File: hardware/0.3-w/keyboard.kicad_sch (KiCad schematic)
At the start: 267 parts, among them J1 USB_C_Receptacle_USB2.0, J2 SWD, J3 JST_PH2, Q1 AO3401A, Q2 2N7002, Q3 2N7002, SW1 RESET, U1 TP4057, U2 SRV05-4, U3 XC6206PxxxMR, U4 nRF52840_holyiot_18010

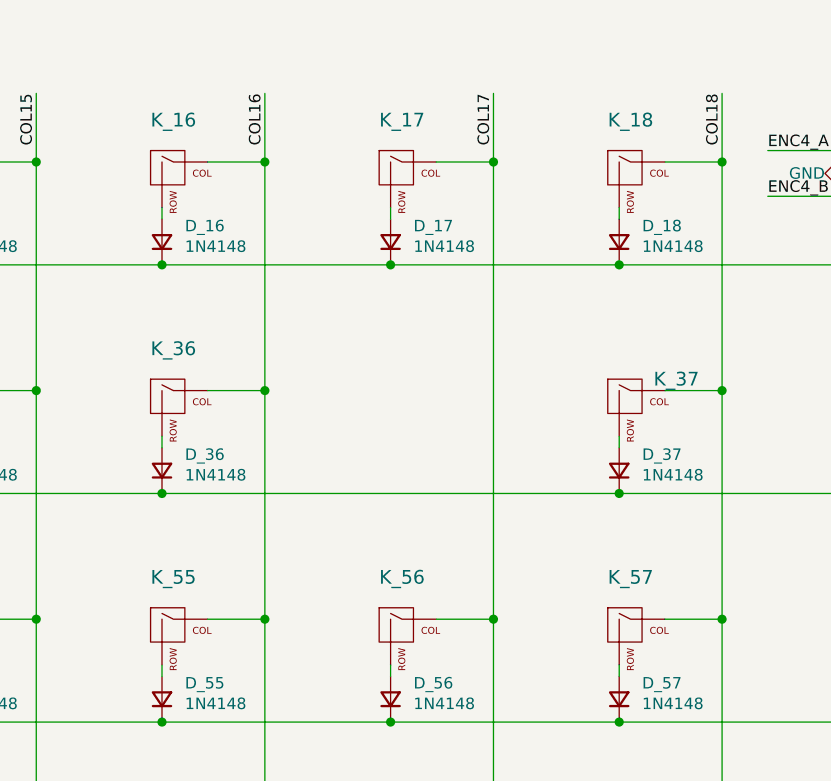
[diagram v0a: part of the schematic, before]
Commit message: all parts placed
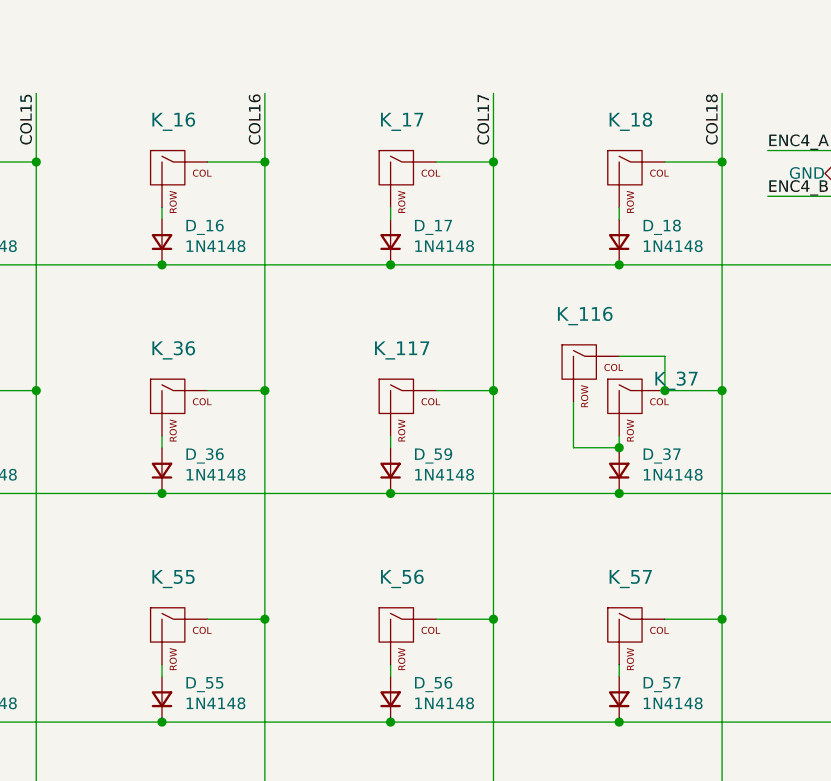
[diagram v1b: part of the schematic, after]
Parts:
- added D_59: 1N4148, Diode_SMD:D_SOD-123, symbol Device:D_Small
- added K_116, K_117: KEYSW, josh-keyboard:MXOnly-1U-NoLED, symbol josh-keyboard:MX-NoLED
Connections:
- net COL17: now also K_117.1 (COL)
- net COL18: now also K_116.1 (COL)
- net ROW1: now also D_59.1 (K)
- net at D_37.2 (A), K_37.2 (ROW): now also K_116.2 (ROW)
- new net: D_59.2 (A), K_117.2 (ROW)
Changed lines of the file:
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@@
   (junction (at 487.68 170.18) (diameter 1.016) (color 0 0 0 0))
   (junction (at 501.65 58.42) (diameter 1.016) (color 0 0 0 0))
+  (junction (at 501.65 83.82) (diameter 1.016) (color 0 0 0 0))
   (junction (at 501.65 109.22) (diameter 1.016) (color 0 0 0 0))
   (junction (at 501.65 134.62) (diameter 1.016) (color 0 0 0 0))
@@
   (junction (at 501.65 185.42) (diameter 1.016) (color 0 0 0 0))
   (junction (at 513.08 46.99) (diameter 1.016) (color 0 0 0 0))
+  (junction (at 513.08 72.39) (diameter 1.016) (color 0 0 0 0))
   (junction (at 513.08 97.79) (diameter 1.016) (color 0 0 0 0))
   (junction (at 513.08 123.19) (diameter 1.016) (color 0 0 0 0))
   (junction (at 513.08 148.59) (diameter 1.016) (color 0 0 0 0))
   (junction (at 527.05 58.42) (diameter 1.016) (color 0 0 0 0))
+  (junction (at 527.05 78.74) (diameter 1.016) (color 0 0 0 0))
   (junction (at 527.05 83.82) (diameter 1.016) (color 0 0 0 0))
   (junction (at 527.05 109.22) (diameter 1.016) (color 0 0 0 0))
   (junction (at 527.05 160.02) (diameter 1.016) (color 0 0 0 0))
   (junction (at 527.05 185.42) (diameter 1.016) (color 0 0 0 0))
+  (junction (at 532.13 72.39) (diameter 1.016) (color 0 0 0 0))
   (junction (at 538.48 46.99) (diameter 1.016) (color 0 0 0 0))
   (junction (at 538.48 72.39) (diameter 1.016) (color 0 0 0 0))
@@
     (stroke (width 0) (type solid) (color 0 0 0 0))
   )
-  (wire (pts (xy 476.25 83.82) (xy 527.05 83.82))
+  (wire (pts (xy 476.25 83.82) (xy 501.65 83.82))
     (stroke (width 0) (type solid) (color 0 0 0 0))
   )
@@
     (stroke (width 0) (type solid) (color 0 0 0 0))
   )
+  (wire (pts (xy 501.65 77.47) (xy 501.65 78.74))
+    (stroke (width 0) (type solid) (color 0 0 0 0))
+  )
+  (wire (pts (xy 501.65 83.82) (xy 527.05 83.82))
+    (stroke (width 0) (type solid) (color 0 0 0 0))
+  )
   (wire (pts (xy 501.65 102.87) (xy 501.65 104.14))
     (stroke (width 0) (type solid) (color 0 0 0 0))
@@
     (stroke (width 0) (type solid) (color 0 0 0 0))
   )
+  (wire (pts (xy 506.73 72.39) (xy 513.08 72.39))
+    (stroke (width 0) (type solid) (color 0 0 0 0))
+  )
   (wire (pts (xy 506.73 97.79) (xy 513.08 97.79))
     (stroke (width 0) (type solid) (color 0 0 0 0))
@@
     (stroke (width 0) (type solid) (color 0 0 0 0))
   )
-  (wire (pts (xy 513.08 46.99) (xy 513.08 97.79))
+  (wire (pts (xy 513.08 46.99) (xy 513.08 72.39))
+    (stroke (width 0) (type solid) (color 0 0 0 0))
+  )
+  (wire (pts (xy 513.08 72.39) (xy 513.08 97.79))
     (stroke (width 0) (type solid) (color 0 0 0 0))
   )
@@
     (stroke (width 0) (type solid) (color 0 0 0 0))
   )
+  (wire (pts (xy 521.97 73.66) (xy 521.97 78.74))
+    (stroke (width 0) (type solid) (color 0 0 0 0))
+  )
+  (wire (pts (xy 521.97 78.74) (xy 527.05 78.74))
+    (stroke (width 0) (type solid) (color 0 0 0 0))
+  )
   (wire (pts (xy 527.05 52.07) (xy 527.05 53.34))
     (stroke (width 0) (type solid) (color 0 0 0 0))
@@
     (stroke (width 0) (type solid) (color 0 0 0 0))
   )
+  (wire (pts (xy 527.05 68.58) (xy 532.13 68.58))
+    (stroke (width 0) (type solid) (color 0 0 0 0))
+  )
   (wire (pts (xy 527.05 77.47) (xy 527.05 78.74))
     (stroke (width 0) (type solid) (color 0 0 0 0))
@@
     (stroke (width 0) (type solid) (color 0 0 0 0))
   )
+  (wire (pts (xy 532.13 68.58) (xy 532.13 72.39))
+    (stroke (width 0) (type solid) (color 0 0 0 0))
+  )
   (wire (pts (xy 532.13 72.39) (xy 538.48 72.39))
     (stroke (width 0) (type solid) (color 0 0 0 0))
@@
     (pin "2")
   )
+  (symbol (lib_id "Device:D_Small") (at 501.65 81.28 90) (unit 1)
+    (in_bom yes) (on_board yes)
+    (property "Reference" "D_59" (id 0) (at 504.19 79.502 90)
+      (effects (font (size 1.27 1.27)) (justify right))
+    )
+    (property "Value" "1N4148" (id 1) (at 504.19 81.788 90)
+      (effects (font (size 1.27 1.27)) (justify right))
+    )
+    (property "Footprint" "Diode_SMD:D_SOD-123" (id 2) (at 502.92 88.9 0)
+      (effects (font (size 1.27 1.27)) hide)
+    )
+    (property "Datasheet" "~" (id 3) (at 502.92 88.9 0)
+      (effects (font (size 1.27 1.27)) hide)
+    )
+    (property "JLCSMT" "C81598" (id 4) (at 501.65 81.28 0)
+      (effects (font (size 1.27 1.27)) hide)
+    )
+    (property "LCSC" "C81598" (id 5) (at 501.65 81.28 0)
+      (effects (font (size 1.27 1.27)) hide)
+    )
+    (property "MPN" "1N4148W" (id 6) (at 501.65 81.28 0)
+      (effects (font (size 1.27 1.27)) hide)
+    )
+    (property "Manufacturer" "Semtech" (id 7) (at 501.65 81.28 0)
+      (effects (font (size 1.27 1.27)) hide)
+    )
+    (pin "1")
+    (pin "2")
+  )
   (symbol (lib_id "Device:D_Small") (at 501.65 106.68 90) (unit 1)
     (in_bom yes) (on_board yes)
@@
     (pin "2")
   )
+  (symbol (lib_id "josh-keyboard:MX-NoLED") (at 502.92 73.66 0) (unit 1)
+    (in_bom yes) (on_board yes)
+    (property "Reference" "K_117" (id 0) (at 502.92 67.7418 0)
+      (effects (font (size 1.524 1.524)))
+    )
+    (property "Value" "KEYSW" (id 1) (at 502.92 76.2 0)
+      (effects (font (size 1.524 1.524)) hide)
+    )
+    (property "Footprint" "josh-keyboard:MXOnly-1U-NoLED" (id 2) (at 502.92 73.66 0)
+      (effects (font (size 1.524 1.524)) hide)
+    )
+    (property "Datasheet" "" (id 3) (at 502.92 73.66 0)
+      (effects (font (size 1.524 1.524)))
+    )
+    (property "DNP" "DNP" (id 4) (at 502.92 73.66 0)
+      (effects (font (size 1.27 1.27)) hide)
+    )
+    (pin "1")
+    (pin "2")
+  )
   (symbol (lib_id "josh-keyboard:MX-NoLED") (at 502.92 99.06 0) (unit 1)
     (in_bom yes) (on_board yes)
@@
     (pin "2")
   )
+  (symbol (lib_id "josh-keyboard:MX-NoLED") (at 523.24 69.85 0) (unit 1)
+    (in_bom yes) (on_board yes)
+    (property "Reference" "K_116" (id 0) (at 523.24 63.9318 0)
+      (effects (font (size 1.524 1.524)))
+    )
+    (property "Value" "KEYSW" (id 1) (at 523.24 72.39 0)
+      (effects (font (size 1.524 1.524)) hide)
+    )
+    (property "Footprint" "josh-keyboard:MXOnly-1U-NoLED" (id 2) (at 523.24 69.85 0)
+      (effects (font (size 1.524 1.524)) hide)
+    )
+    (property "Datasheet" "" (id 3) (at 523.24 69.85 0)
+      (effects (font (size 1.524 1.524)))
+    )
+    (property "DNP" "DNP" (id 4) (at 523.24 69.85 0)
+      (effects (font (size 1.27 1.27)) hide)
+    )
+    (pin "1")
+    (pin "2")
+  )
   (symbol (lib_id "josh-keyboard:MX-NoLED") (at 528.32 48.26 0) (unit 1)
     (in_bom yes) (on_board yes)
@@
       (reference "D_58") (unit 1) (value "1N4148") (footprint "Diode_SMD:D_SOD-123")
     )
+    (path "/cb42b9bb-fc46-4c19-b315-048646672a96"
+      (reference "D_59") (unit 1) (value "1N4148") (footprint "Diode_SMD:D_SOD-123")
+    )
     (path "/00000000-0000-0000-0000-000000000600"
       (reference "D_60") (unit 1) (value "1N4148") (footprint "Diode_SMD:D_SOD-123")
@@
       (reference "K_115") (unit 1) (value "KEYSW") (footprint "josh-keyboard:MXOnly-1U-NoLED")
     )
+    (path "/a53bcfa5-987c-4dbc-9743-d5bb1d285c81"
+      (reference "K_116") (unit 1) (value "KEYSW") (footprint "josh-keyboard:MXOnly-1U-NoLED")
+    )
+    (path "/3eab3946-b5c2-4325-8805-84ddc6f65b8a"
+      (reference "K_117") (unit 1) (value "KEYSW") (footprint "josh-keyboard:MXOnly-1U-NoLED")
+    )
     (path "/00000000-0000-0000-0000-0000619339fa"

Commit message: drc = erc = 0
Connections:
- net COL0: now also U4.36 (P0.10)
- net COL1: now also U4.6 (P0.03)
- net COL10: now also U4.27 (P1.00)
- net COL11: now also U4.26 (P0.22)
- net COL12: now also U4.39 (P1.12)
- net COL13: now also U4.47 (P1.07)
- net COL14: now also U4.48 (P1.05)
- net COL15: now also U4.34 (P1.06)
- net COL16: now also U4.49 (P0.24)
- net COL17: now also U4.33 (P1.04)
- net COL18: now also U4.50 (P0.20)
- net COL19: now also U4.51 (P0.17)
- net COL2: now also U4.15 (P0.07)
- net COL3: now also U4.16 (P1.09)
- net COL4: now also U4.35 (P0.09)
- net COL5: now also U4.38 (P1.14)
- net COL6: now also U4.30 (P1.02)
- net COL7: now also U4.29 (P1.01)
- net COL8: now also U4.53 (P0.14)
- net COL9: now also U4.28 (P1.03)
- net ENC0_A: now also U4.7 (P0.02)
- net ENC0_B: now also U4.8 (P0.28)
- net ENC1_A: now also U4.9 (P0.29)
- net ENC1_B: now also U4.10 (P0.30)
- net ENC2_A: now also U4.17 (P0.12)
- net ENC2_B: now also U4.18 (P0.23)
- net ENC3_A: now also U4.19 (P0.21)
- net ENC3_B: now also U4.20 (P0.19)
- net ENC4_A: now also U4.55 (P0.16)
- net ENC4_B: now also U4.54 (P0.13)
- net ROW0: now also U4.46 (P0.26)
- net ROW1: now also U4.45 (P0.06)
- net ROW2: now also U4.43 (P0.27)
- net ROW3: now also U4.42 (P1.08)
- net ROW4: now also U4.41 (P0.11)
- net ROW5: now also U4.40 (P0.25)
- no-connect marks 4 -> 11

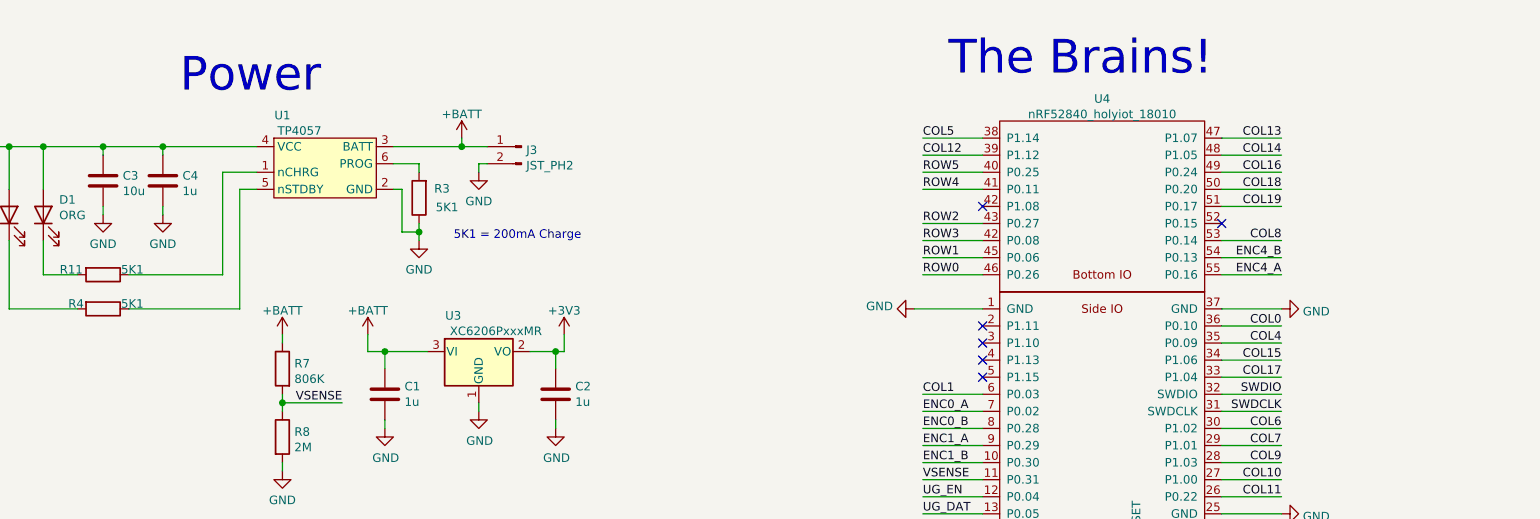
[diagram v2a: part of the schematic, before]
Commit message: added user led
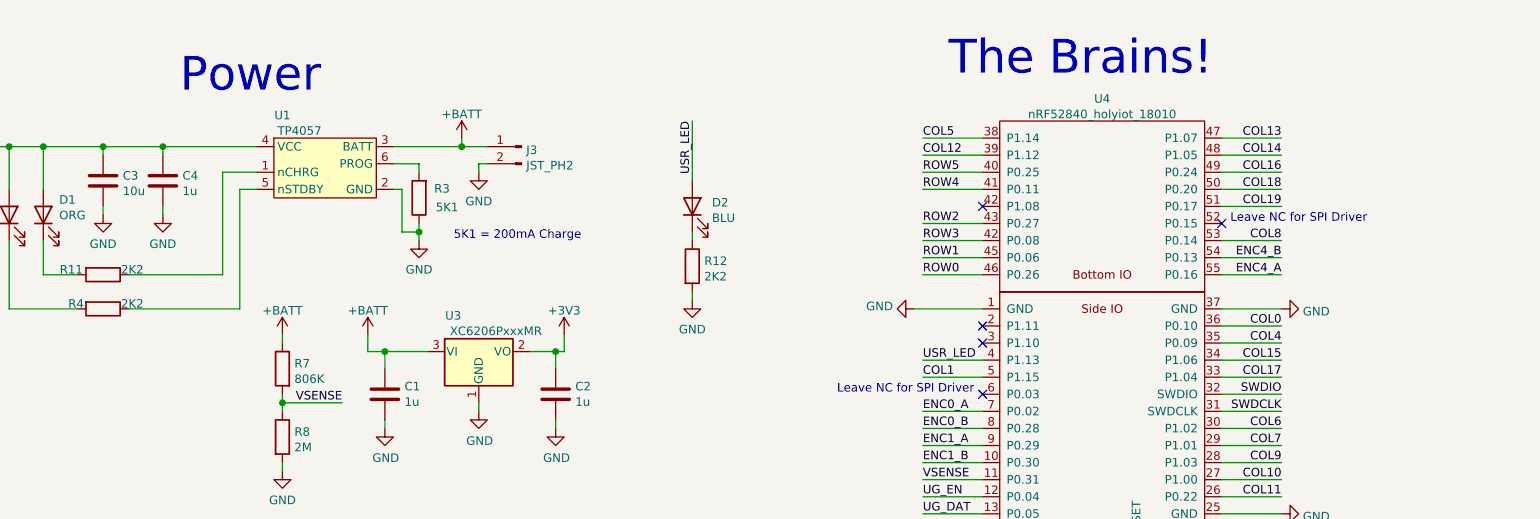
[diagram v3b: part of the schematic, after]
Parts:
- added D2: BLU, LED_SMD:LED_0603_1608Metric, symbol Device:LED
- added R12: 2K2, Resistor_SMD:R_0603_1608Metric, symbol Device:R
- R11, R4: value 5K1 -> 2K2
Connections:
- net COL1: now also U4.5 (P1.15); no longer U4.6 (P0.03)
- net GND: now also R12.2
- net USR_LED: now reaches U4.4 (P1.13)
- net USR_LED: now also D2.2 (A)
- new net: D2.1 (K), R12.1
- no-connect marks 11 -> 10
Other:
- note added: "Leave NC for SPI Driver"
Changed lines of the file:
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@@
   (no_connect (at 350.52 265.43))
   (no_connect (at 350.52 267.97))
-  (no_connect (at 350.52 270.51))
-  (no_connect (at 350.52 273.05))
+  (no_connect (at 350.52 275.59))
   (no_connect (at 386.08 250.19))
   (wire (pts (xy 35.56 46.99) (xy 27.94 46.99))
@@
     (stroke (width 0) (type solid) (color 0 0 0 0))
   )
+  (wire (pts (xy 307.34 234.95) (xy 307.34 243.84))
+    (stroke (width 0) (type solid) (color 0 0 0 0))
+  )
+  (wire (pts (xy 307.34 251.46) (xy 307.34 252.73))
+    (stroke (width 0) (type solid) (color 0 0 0 0))
+  )
+  (wire (pts (xy 307.34 260.35) (xy 307.34 261.62))
+    (stroke (width 0) (type solid) (color 0 0 0 0))
+  )
   (wire (pts (xy 309.88 39.37) (xy 309.88 46.99))
     (stroke (width 0) (type solid) (color 0 0 0 0))
@@
     (stroke (width 0) (type solid) (color 0 0 0 0))
   )
+  (wire (pts (xy 341.63 270.51) (xy 350.52 270.51))
+    (stroke (width 0) (type solid) (color 0 0 0 0))
+  )
   (wire (pts (xy 341.63 278.13) (xy 350.52 278.13))
     (stroke (width 0) (type solid) (color 0 0 0 0))
@@
     (stroke (width 0) (type solid) (color 0 0 0 0))
   )
-  (wire (pts (xy 350.52 275.59) (xy 341.63 275.59))
+  (wire (pts (xy 350.52 273.05) (xy 341.63 273.05))
     (stroke (width 0) (type solid) (color 0 0 0 0))
   )
@@
     (effects (font (size 5.0038 5.0038)) (justify left bottom))
   )
+  (text "Leave NC for SPI Driver" (at 349.25 275.59 180)
+    (effects (font (size 1.27 1.27)) (justify right bottom))
+  )
   (text "Logos / Silk" (at 372.11 375.92 0)
     (effects (font (size 2.54 2.54)) (justify left bottom))
   )
+  (text "Leave NC for SPI Driver" (at 387.35 250.19 0)
+    (effects (font (size 1.27 1.27)) (justify left bottom))
+  )
   (text "Stopping \nERC Errors" (at 402.59 378.46 0)
     (effects (font (size 2.54 2.54)) (justify left bottom))
@@
     (effects (font (size 1.27 1.27)) (justify right bottom))
   )
+  (label "USR_LED" (at 307.34 234.95 270)
+    (effects (font (size 1.27 1.27)) (justify right bottom))
+  )
   (label "COL9" (at 309.88 39.37 270)
     (effects (font (size 1.27 1.27)) (justify right bottom))
@@
     (effects (font (size 1.27 1.27)) (justify left bottom))
   )
-  (label "COL1" (at 341.63 275.59 0)
+  (label "USR_LED" (at 341.63 270.51 0)
+    (effects (font (size 1.27 1.27)) (justify left bottom))
+  )
+  (label "COL1" (at 341.63 273.05 0)
     (effects (font (size 1.27 1.27)) (justify left bottom))
   )
@@
     (pin "1")
   )
+  (symbol (lib_id "power:GND") (at 307.34 261.62 0) (unit 1)
+    (in_bom yes) (on_board yes) (fields_autoplaced)
+    (property "Reference" "#PWR0134" (id 0) (at 307.34 267.97 0)
+      (effects (font (size 1.27 1.27)) hide)
+    )
+    (property "Value" "GND" (id 1) (at 307.34 265.9444 0))
+    (property "Footprint" "" (id 2) (at 307.34 261.62 0)
+      (effects (font (size 1.27 1.27)) hide)
+    )
+    (property "Datasheet" "" (id 3) (at 307.34 261.62 0)
+      (effects (font (size 1.27 1.27)) hide)
+    )
+    (pin "1")
+  )
   (symbol (lib_id "power:GND") (at 340.36 262.89 270) (unit 1)
     (in_bom yes) (on_board yes) (fields_autoplaced)
@@
       (effects (font (size 1.27 1.27)) (justify left))
     )
-    (property "Value" "5K1" (id 1) (at 222.377 257.048 90)
+    (property "Value" "2K2" (id 1) (at 222.377 257.048 90)
       (effects (font (size 1.27 1.27)) (justify left))
     )
@@
       (effects (font (size 1.27 1.27)) (justify left))
     )
-    (property "Value" "5K1" (id 1) (at 222.377 262.128 90)
+    (property "Value" "2K2" (id 1) (at 222.377 262.128 90)
       (effects (font (size 1.27 1.27)) (justify left))
     )
@@
     (pin "2")
   )
+  (symbol (lib_id "Device:R") (at 307.34 256.54 0) (unit 1)
+    (in_bom yes) (on_board yes) (fields_autoplaced)
+    (property "Reference" "R12" (id 0) (at 309.1181 255.7791 0)
+      (effects (font (size 1.27 1.27)) (justify left))
+    )
+    (property "Value" "2K2" (id 1) (at 309.1181 258.0778 0)
+      (effects (font (size 1.27 1.27)) (justify left))
+    )
+    (property "Footprint" "Resistor_SMD:R_0603_1608Metric" (id 2) (at 305.562 256.54 90)
+      (effects (font (size 1.27 1.27)) hide)
+    )
+    (property "Datasheet" "~" (id 3) (at 307.34 256.54 0)
+      (effects (font (size 1.27 1.27)) hide)
+    )
+    (pin "1")
+    (pin "2")
+  )
   (symbol (lib_id "Device:Polyfuse") (at 176.53 238.76 270) (unit 1)
     (in_bom yes) (on_board yes)
@@
     (pin "2")
   )
+  (symbol (lib_id "Device:LED") (at 307.34 247.65 90) (unit 1)
+    (in_bom yes) (on_board yes) (fields_autoplaced)
+    (property "Reference" "D2" (id 0) (at 310.2611 247.0796 90)
+      (effects (font (size 1.27 1.27)) (justify right))
+    )
+    (property "Value" "BLU" (id 1) (at 310.2611 249.3783 90)
+      (effects (font (size 1.27 1.27)) (justify right))
+    )
+    (property "Footprint" "LED_SMD:LED_0603_1608Metric" (id 2) (at 307.34 247.65 0)
+      (effects (font (size 1.27 1.27)) hide)
+    )
+    (property "Datasheet" "~" (id 3) (at 307.34 247.65 0)
+      (effects (font (size 1.27 1.27)) hide)
+    )
+    (pin "1")
+    (pin "2")
+  )
   (symbol (lib_id "Device:C") (at 151.13 233.68 270) (unit 1)
     (in_bom yes) (on_board yes)
@@
       (reference "#PWR0133") (unit 1) (value "GND") (footprint "")
     )
+    (path "/379ff50b-b9de-4a18-9476-6322dce26667"
+      (reference "#PWR0134") (unit 1) (value "GND") (footprint "")
+    )
     (path "/00000000-0000-0000-0000-0000704c489d"
       (reference "#PWR0142") (unit 1) (value "GND") (footprint "")
@@
       (reference "D1") (unit 1) (value "ORG") (footprint "LED_SMD:LED_0603_1608Metric")
     )
+    (path "/58feb3e0-5b67-4960-9ce9-f4d263ded301"
+      (reference "D2") (unit 1) (value "BLU") (footprint "LED_SMD:LED_0603_1608Metric")
+    )
     (path "/00000000-0000-0000-0000-00005ef17407"
       (reference "D14") (unit 1) (value "PINK") (footprint "LED_SMD:LED_0603_1608Metric")
@@
     )
     (path "/678f5bb1-ec18-4735-be7a-0790713e27a9"
-      (reference "R4") (unit 1) (value "5K1") (footprint "Resistor_SMD:R_0603_1608Metric")
+      (reference "R4") (unit 1) (value "2K2") (footprint "Resistor_SMD:R_0603_1608Metric")
     )
     (path "/00000000-0000-0000-0000-00006978ccf4"
@@
     )
     (path "/00000000-0000-0000-0000-00005ef14b61"
-      (reference "R11") (unit 1) (value "5K1") (footprint "Resistor_SMD:R_0603_1608Metric")
+      (reference "R11") (unit 1) (value "2K2") (footprint "Resistor_SMD:R_0603_1608Metric")
+    )
+    (path "/d132ba32-0eeb-435b-9a0d-bc2043fac992"
+      (reference "R12") (unit 1) (value "2K2") (footprint "Resistor_SMD:R_0603_1608Metric")
     )
     (path "/00000000-0000-0000-0000-00006825bd47"
